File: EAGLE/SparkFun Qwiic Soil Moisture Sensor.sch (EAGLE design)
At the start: 14 parts, among them J1 JST-SH-4P-1.0, J2 JST-SH-4P-1.0, U1 Tiny85-20-SMT

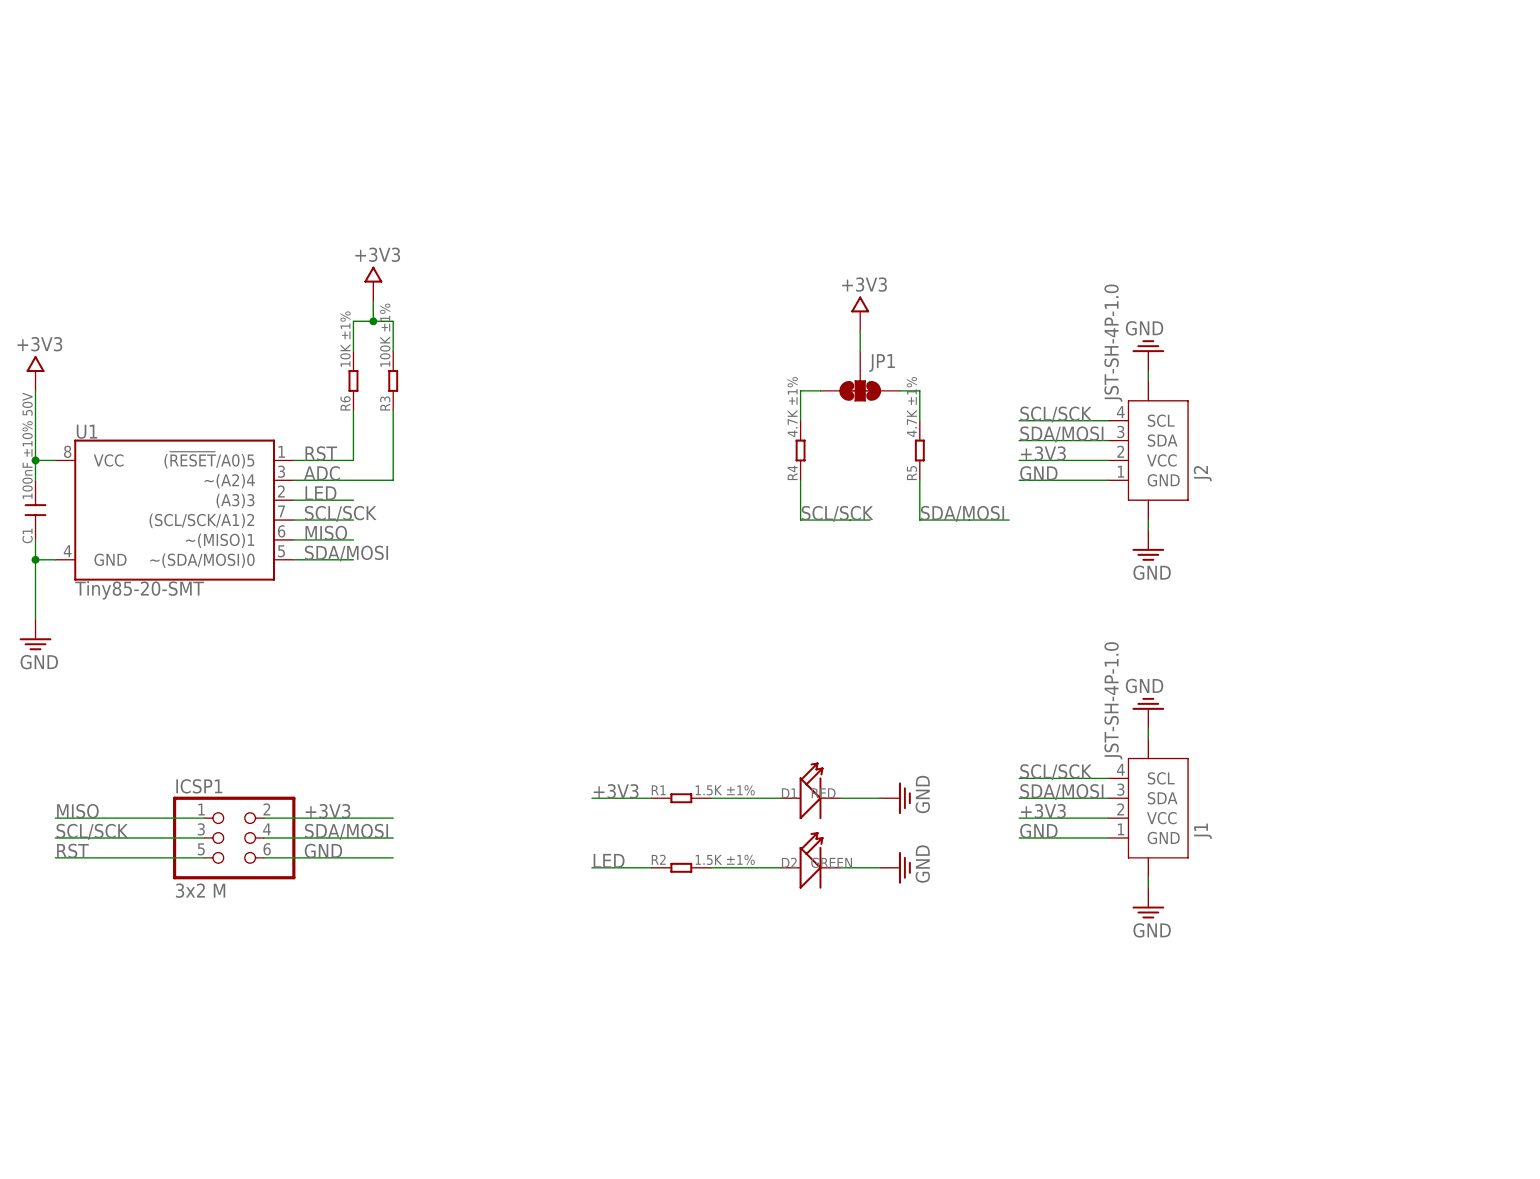
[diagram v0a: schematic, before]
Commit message: Update SparkFun Qwiic Soil Moisture Sensor.sch
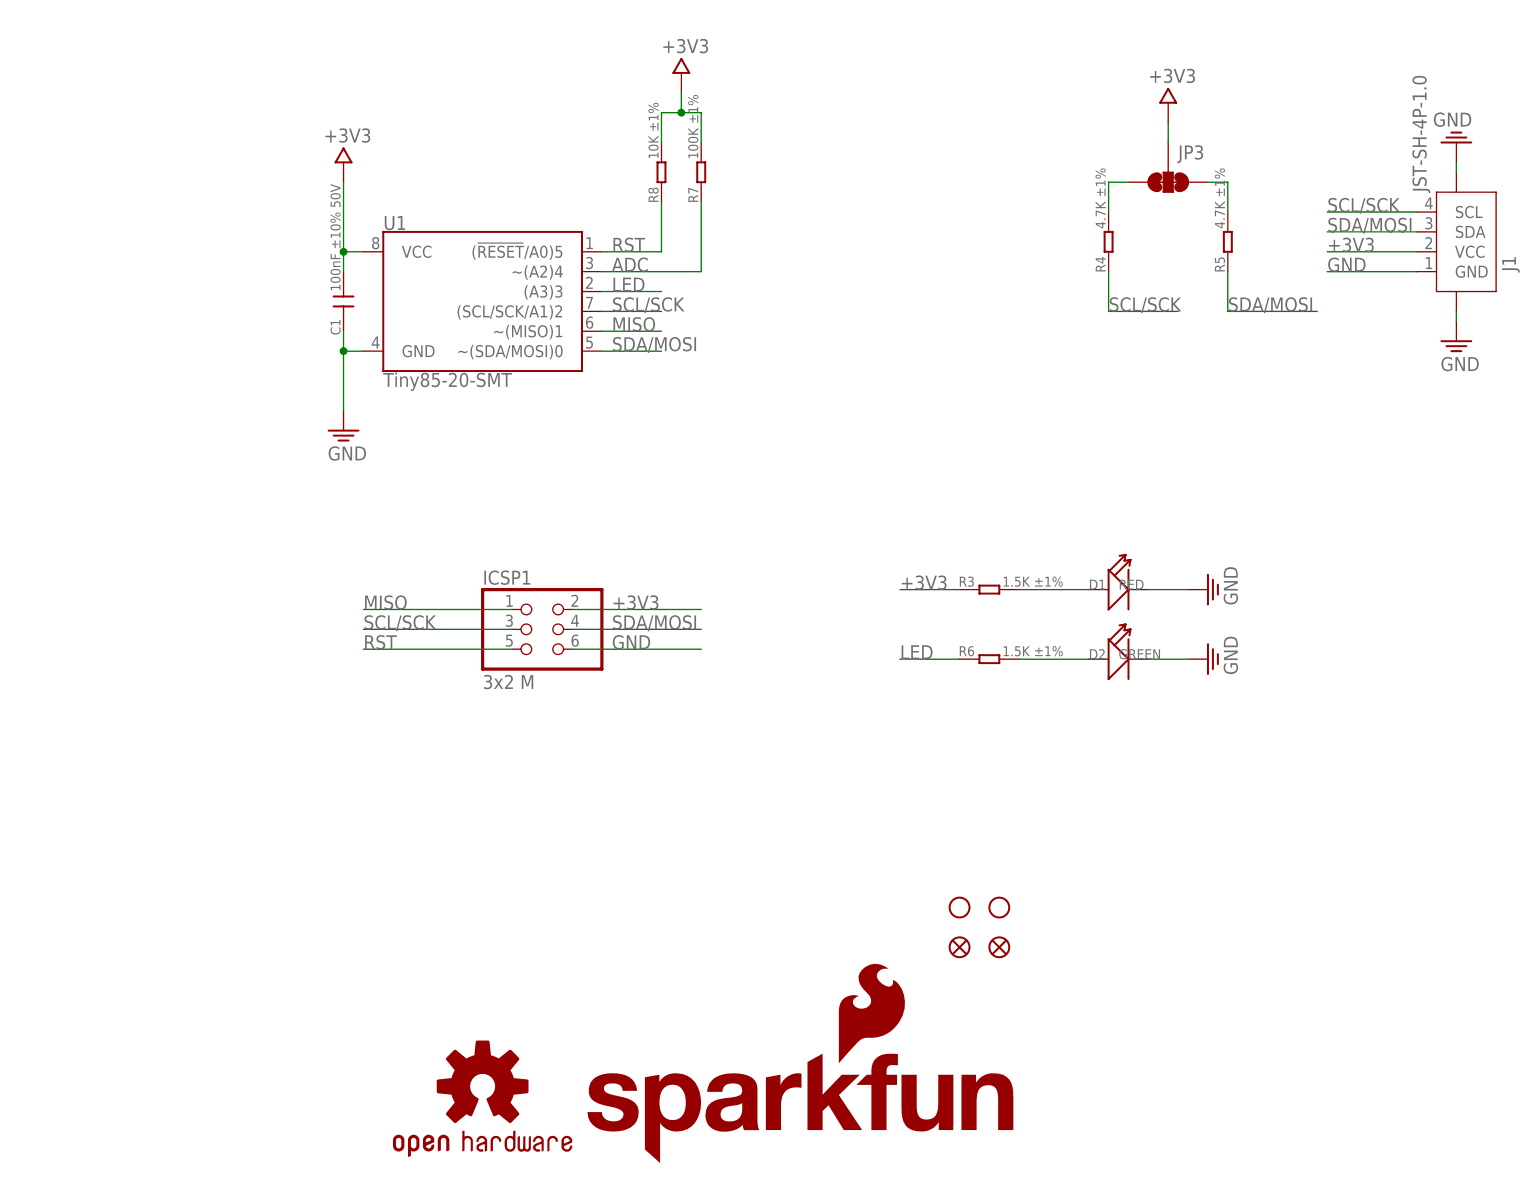
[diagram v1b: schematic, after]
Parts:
- removed J2: JST-SH-4P-1.0, Connector:JST-SH-4P-1.0
- removed JP1: SMT-JUMPER_3_2-NC_TRACE, NOA-Jumpers:SMT-JUMPER_3_2-NC_TRACE
- removed R1, R2: 1.5K ±1%, RCL:R-0603
- added FID1, FID2: FIDUCIAL1X2, SparkFun-Aesthetics:FIDUCIAL1X2
- added JP3: SMT-JUMPER_3_2-NC_TRACE, NOA-Jumpers:SMT-JUMPER_3_2-NC_TRACE
- added LOGO1: SFE_LOGO_NAME_FLAME.1_INCH, SparkFun-Aesthetics:SFE_LOGO_NAME_FLAME.1_INCH
- added LOGO2: OSHW-LOGOS, SparkFun-Aesthetics:OSHW-LOGOS
- added R7: 100K ±1%, RCL:R-0603
- added R8: 10K ±1%, RCL:R-0603
- added STANDOFF1, STANDOFF2: STAND-OFF, SparkFun-Electromechanical:STAND-OFF
- R3: value 100K ±1% -> 1.5K ±1%
- R6: value 10K ±1% -> 1.5K ±1%
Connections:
- net +3V3: now also JP3.2, R3.1, R7.2, R8.2; no longer J2.VCC, JP1.2, R1.1, R3.2, R6.2
- net ADC: now also R7.1; no longer R3.1
- net GND: no longer J2.5, J2.6, J2.GND
- net LED: now also R6.1; no longer R2.1
- net N$1: now also R3.2; no longer R1.2
- net N$2: now also R6.2; no longer R2.2
- net N$6: now also JP3.3; no longer JP1.3
- net N$8: now also JP3.1; no longer JP1.1
- net RST: now also R8.1; no longer R6.1
- net SCL/SCK: no longer J2.SCL
- net SDA/MOSI: no longer J2.SDA
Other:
- moved on the sheet: C1, D1, D2, ICSP1, J1, R3, R4, R5, R6, U1
